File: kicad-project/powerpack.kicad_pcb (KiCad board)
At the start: 2 copper layers, 16.9 x 32.9 mm, 10 parts, among them J1 Power_in 3.3-15V, J2.1 Vout +3.3V, J2.2 Vout GND, U1 MCP1703T-3302E_CB

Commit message: Update
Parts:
- removed the G*** at (171.8, 41.8)
- removed REF**: OSHW-Logo2_14.6x12mm_SilkScreen, Symbol:OSHW-Logo2_14.6x12mm_SilkScreen
- added G***: LOGO, logo:attnode_logo_sml_silk, F.Cu at (169.8, 25.8)
- added J4: ADC, TestPoint:TestPoint_Pad_2.5x2.5mm, F.Cu at (168.9, 41.7)
- added R1: R, Resistor_SMD:R_1206_3216Metric_Pad1.30x1.75mm_HandSolder, F.Cu at (174.2, 40.2)
- added R2: R, Resistor_SMD:R_1206_3216Metric_Pad1.30x1.75mm_HandSolder, F.Cu at (174.2, 43.5)
- C1, C2: value 1uF -> 1µF
- J3.1: renamed from +; value Vin 3.3V-15V -> Vin
- J3.2: renamed from -; value Vin GND -> GND
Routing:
- net Net-(J4-Pad1): track 0.00 -> 8.99 mm
- net GND: track 39.8 -> 46.7 mm
- net VCC: track 39.9 -> 42.0 mm
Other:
- board text added: "powerpack v1.1 attno.de"
- board text removed: "powerpack v1.0 attno.de"

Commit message: update Silk and folder
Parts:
- added REF**: KiCad-Logo2_6mm_SilkScreen, Symbol:KiCad-Logo2_6mm_SilkScreen, B.Cu at (169.7, 35.4)
- added REF**: OSHW-Logo2_7.3x6mm_SilkScreen, Symbol:OSHW-Logo2_7.3x6mm_SilkScreen, B.Cu at (178.5, 35.8)

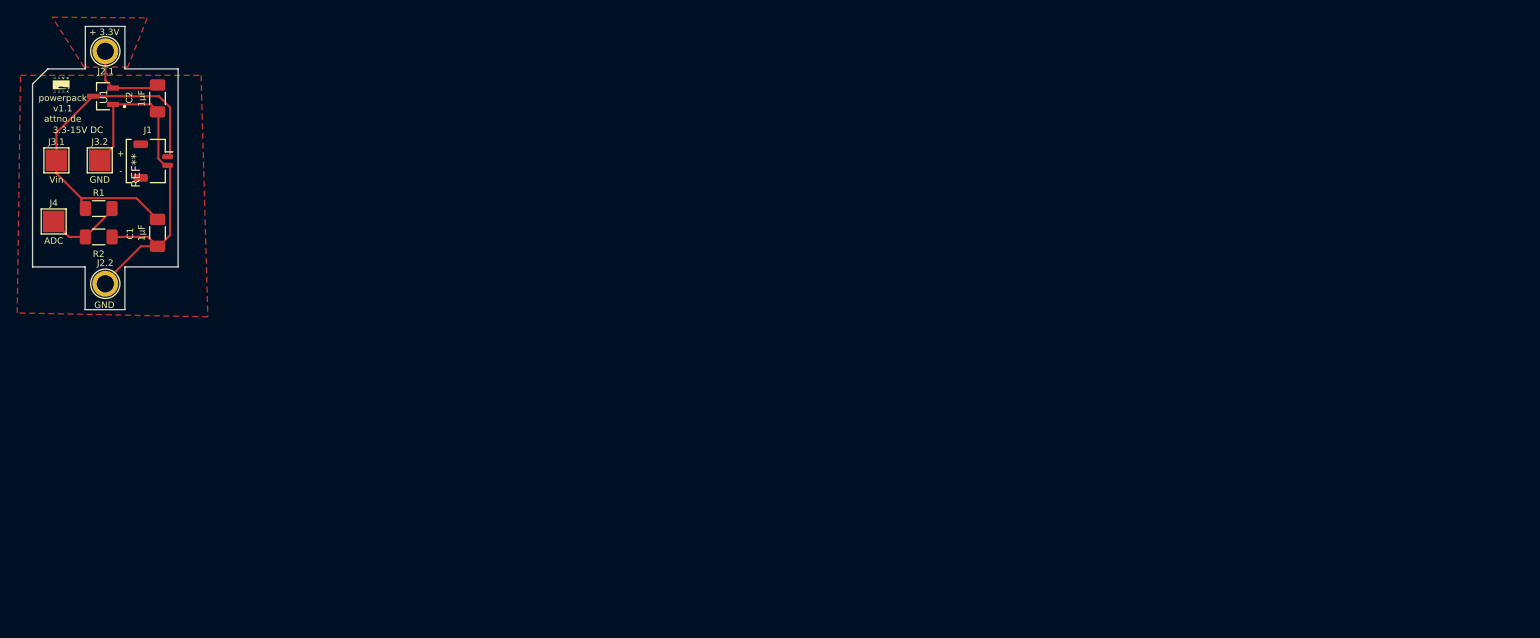
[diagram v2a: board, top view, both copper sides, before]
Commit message: Added Support USB-C
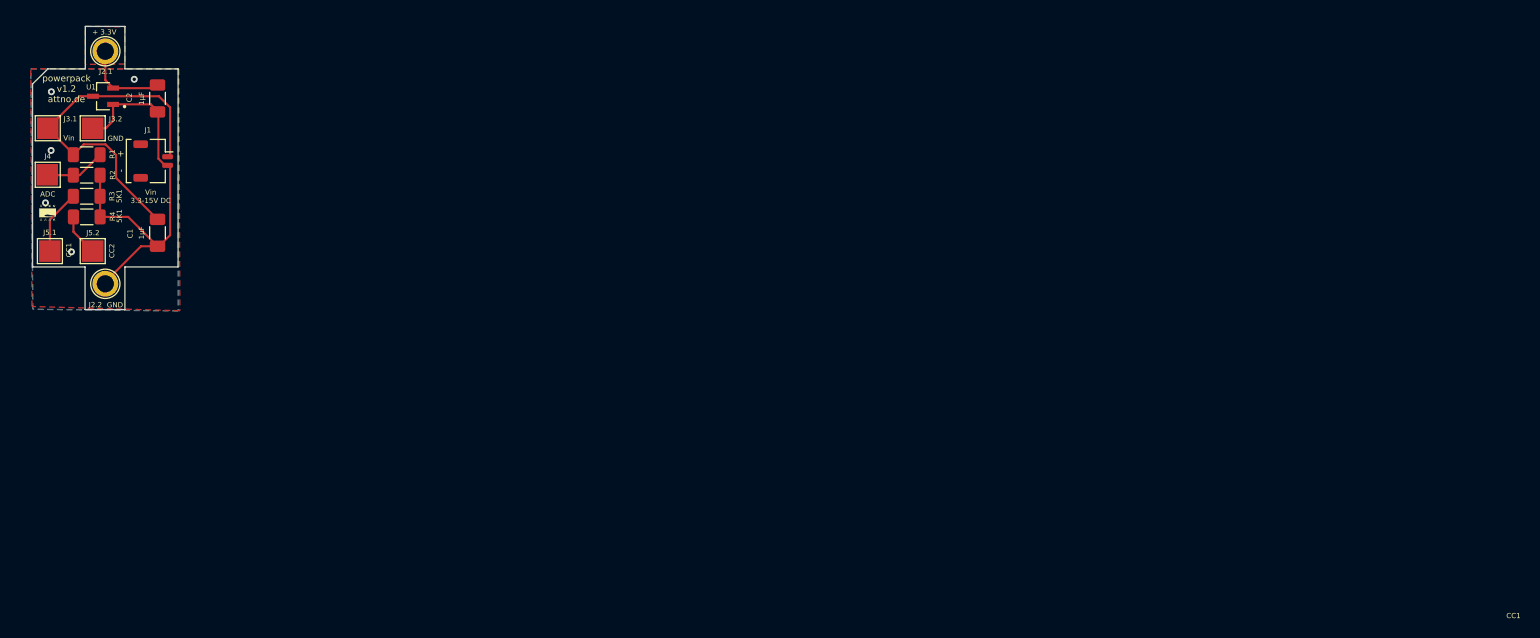
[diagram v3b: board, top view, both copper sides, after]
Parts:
- added ?: , , F.Cu at (176.0, 45.3)
- added ?: , , F.Cu at (168.6, 40.8)
- added J5.1: CC1, TestPoint:TestPoint_Pad_2.5x2.5mm, F.Cu at (168.5, 45.1)
- added J5.2: CC2, TestPoint:TestPoint_Pad_2.5x2.5mm, F.Cu at (173.5, 45.1)
- added R3: 5K1, Resistor_SMD:R_1206_3216Metric_Pad1.30x1.75mm_HandSolder, F.Cu at (172.8, 38.7)
- added R4: 5K1, Resistor_SMD:R_1206_3216Metric_Pad1.30x1.75mm_HandSolder, F.Cu at (172.8, 41.1)
- moved G*** 14.9 mm to (168.2, 40.7)
- moved R2 7.30 mm to (172.8, 36.3)
- moved R1 6.40 mm to (172.8, 33.9)
- moved J4 5.46 mm to (168.3, 36.2)
- moved J3.1 3.86 mm to (168.3, 30.8)
- moved J3.2 3.81 mm to (173.5, 30.9)
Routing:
- net Net-(J5.1-Pad1): track 0.00 -> 7.49 mm
- net Net-(J5.2-Pad1): track 0.00 -> 4.90 mm
- net GND: track 46.7 -> 51.3 mm, vias 0 -> 5
- net Net-(J4-Pad1): track 8.99 -> 7.13 mm
- added copper zone on B.Cu, net GND
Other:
- board text added: "CC2"
- board text added: "Vin 3.3-15V DC"
- board text added: "powerpack v1.2 attno.de"
- board text removed: "3.3-15V DC"
- board text removed: "powerpack v1.1 attno.de"
